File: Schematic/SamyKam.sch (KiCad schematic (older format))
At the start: 16 parts, among them IC1 ATTINY85-P, P1 OLED, U1 TC4424, U2 RPi_A+_B+_2B_Hat

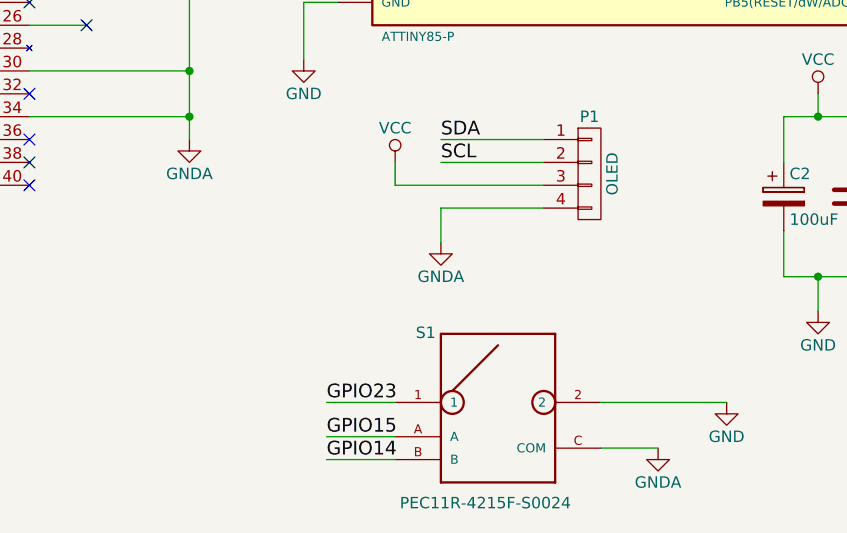
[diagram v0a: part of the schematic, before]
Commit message: Fix Connection Grounds
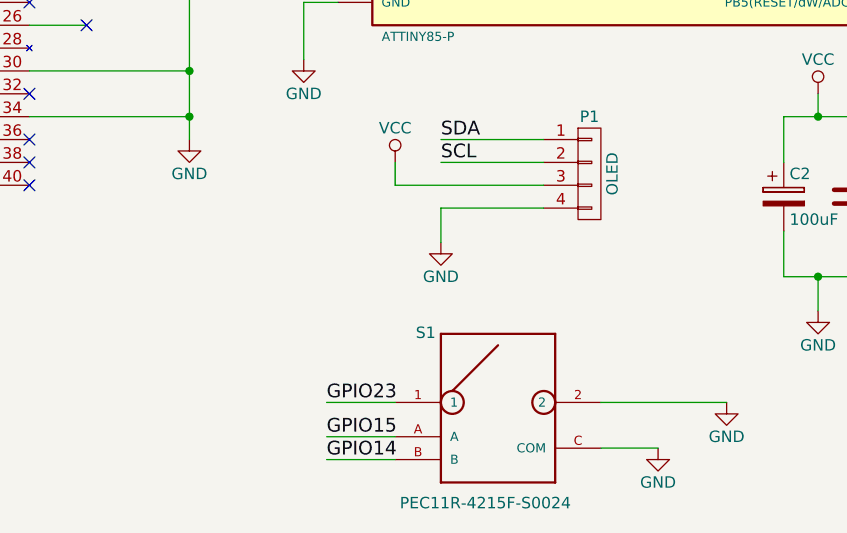
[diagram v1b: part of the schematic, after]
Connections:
- net GNDA is gone; now on net GND: P1.4 (P4), S1.C (COM), U2.30 (GND), U2.34 (GND), U2.6 (GND)
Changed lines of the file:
@@
 NoConn ~ 2300 3300
-$Comp
-L GNDA #PWR015
-U 1 1 58548963
-P 4300 3500
-F 0 "#PWR015" H 4300 3250 50  0001 C CNN
-F 1 "GNDA" H 4300 3350 50  0000 C CNN
-F 2 "" H 4300 3500 50  0000 C CNN
-F 3 "" H 4300 3500 50  0000 C CNN
-	1    4300 3500
-	1    0    0    -1
-$EndComp
-$Comp
-L GNDA #PWR016
-U 1 1 58548ABC
-P 6350 4850
-F 0 "#PWR016" H 6350 4600 50  0001 C CNN
-F 1 "GNDA" H 6350 4700 50  0000 C CNN
-F 2 "" H 6350 4850 50  0000 C CNN
-F 3 "" H 6350 4850 50  0000 C CNN
-	1    6350 4850
-	1    0    0    -1
-$EndComp
-$Comp
-L GNDA #PWR017
-U 1 1 58549023
-P 5400 3950
-F 0 "#PWR017" H 5400 3700 50  0001 C CNN
-F 1 "GNDA" H 5400 3800 50  0000 C CNN
-F 2 "" H 5400 3950 50  0000 C CNN
-F 3 "" H 5400 3950 50  0000 C CNN
-	1    5400 3950
-	1    0    0    -1
-$EndComp
 $Comp
 L RPi_A+_B+_2B_Hat U2
@@
 Wire Wire Line
 	1850 2600 2500 2600
+$Comp
+L GND #PWR?
+U 1 1 58927C2F
+P 4300 3500
+F 0 "#PWR?" H 4300 3250 50  0001 C CNN
+F 1 "GND" H 4300 3350 50  0000 C CNN
+F 2 "" H 4300 3500 50  0000 C CNN
+F 3 "" H 4300 3500 50  0000 C CNN
+	1    4300 3500
+	1    0    0    -1
+$EndComp
+$Comp
+L GND #PWR?
+U 1 1 58927EE4
+P 6350 4850
+F 0 "#PWR?" H 6350 4600 50  0001 C CNN
+F 1 "GND" H 6350 4700 50  0000 C CNN
+F 2 "" H 6350 4850 50  0000 C CNN
+F 3 "" H 6350 4850 50  0000 C CNN
+	1    6350 4850
+	1    0    0    -1
+$EndComp
+$Comp
+L GND #PWR?
+U 1 1 589284A9
+P 5400 3950
+F 0 "#PWR?" H 5400 3700 50  0001 C CNN
+F 1 "GND" H 5400 3800 50  0000 C CNN
+F 2 "" H 5400 3950 50  0000 C CNN
+F 3 "" H 5400 3950 50  0000 C CNN
+	1    5400 3950
+	1    0    0    -1
+$EndComp
 $EndSCHEMATC
